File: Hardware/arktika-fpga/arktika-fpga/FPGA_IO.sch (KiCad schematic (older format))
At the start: 12 parts

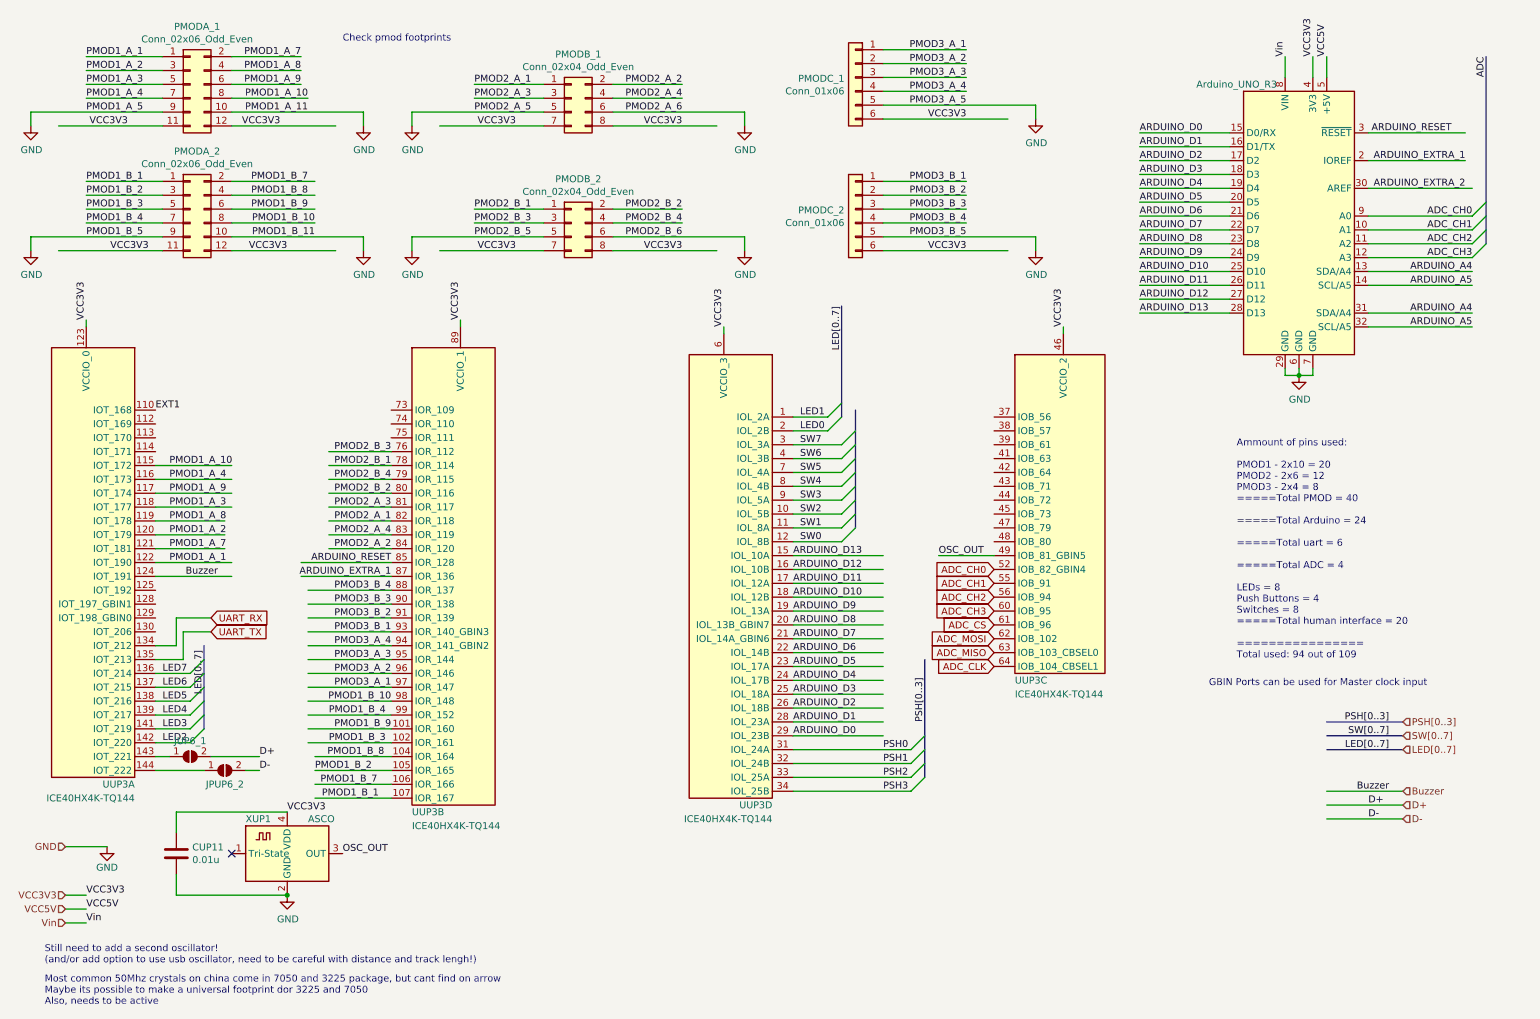
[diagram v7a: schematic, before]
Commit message: Added more IO
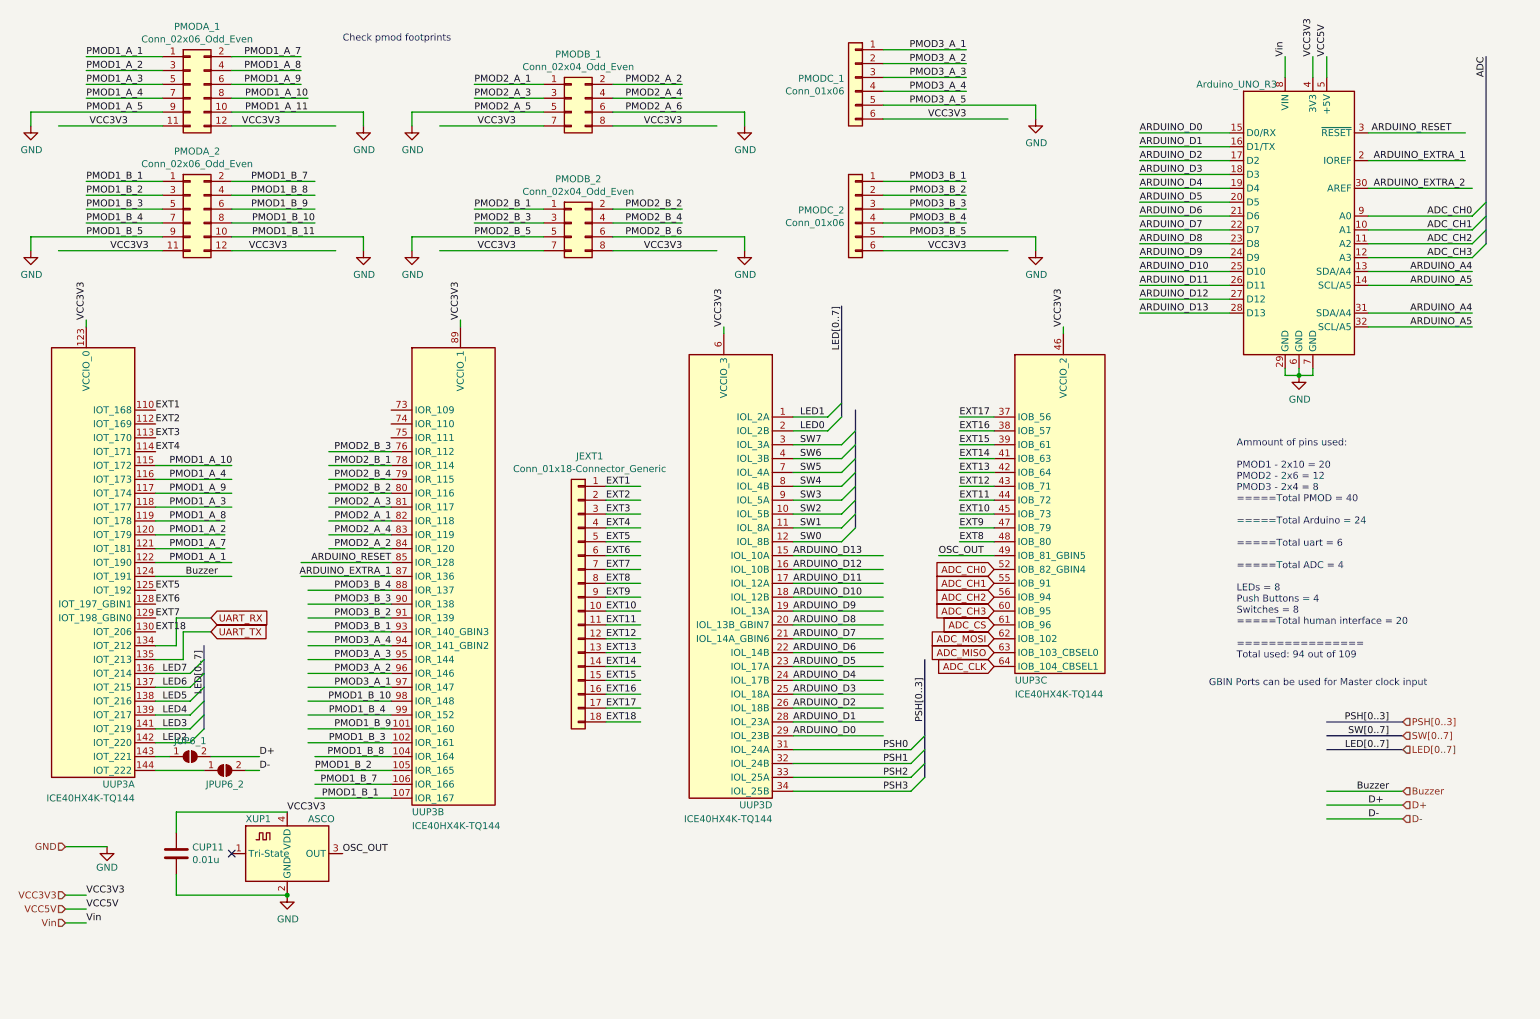
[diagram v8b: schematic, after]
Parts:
- added JEXT1: Conn_01x18-Connector_Generic, Connector_PinHeader_2.54mm:PinHeader_1x18_P2.54mm_Vertical, symbol arktika-fpga-rescue:Conn_01x18-Connector_Generic
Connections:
- net labels added: EXT10, EXT11, EXT12, EXT13, EXT14, EXT15, EXT16, EXT17, EXT18, EXT2, EXT3, EXT4, EXT5, EXT6, EXT7, EXT8, EXT9
- wire segments 190 -> 218
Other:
- note removed: "Most common 50Mhz crystals on china come in 7050 and 3225 package, but cant find on arrow\nMaybe its possible to make a universal footprint dor 3225 and 7050\nAlso, needs to be active"
- note removed: "Still need to add a second oscillator!\n(and/or add option to use usb oscillator, need to be careful with distance and track lengh!)"
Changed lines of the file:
@@
 Wire Wire Line
 	10000 800  10000 950
-Text Notes 750  7350 0    50   ~ 0
-Still need to add a second oscillator!\n(and/or add option to use usb oscillator, need to be careful with distance and track lengh!)
-Text Notes 750  7650 0    50   ~ 0
-Most common 50Mhz crystals on china come in 7050 and 3225 package, but cant find on arrow\nMaybe its possible to make a universal footprint dor 3225 and 7050\nAlso, needs to be active
 $Comp
 L arktika-fpga-rescue:ASCO-Oscillator XUP1
@@
 Text Label 3250 3850 2    50   ~ 0
 PMOD2_B_4
+Text Label 2500 6250 0    50   ~ 0
+VCC3V3
+Text Label 2450 1300 2    50   ~ 0
+VCC3V3
+Text Label 1350 1300 2    50   ~ 0
+VCC3V3
+Text Label 1500 2200 2    50   ~ 0
+VCC3V3
+Text Label 2500 2200 2    50   ~ 0
+VCC3V3
+Text Label 4150 2200 2    50   ~ 0
+VCC3V3
+Text Label 5350 2200 2    50   ~ 0
+VCC3V3
+Text Label 5350 1300 2    50   ~ 0
+VCC3V3
+Text Label 4150 1300 2    50   ~ 0
+VCC3V3
+Text Label 7400 1250 2    50   ~ 0
+VCC3V3
+Text Label 7400 2200 2    50   ~ 0
+VCC3V3
+Text Label 1550 3450 0    50   ~ 0
+EXT2
+Text Label 1550 3550 0    50   ~ 0
+EXT3
+Text Label 1550 3650 0    50   ~ 0
+EXT4
+Text Label 1550 4650 0    50   ~ 0
+EXT5
+Text Label 1550 4750 0    50   ~ 0
+EXT6
+Text Label 1550 4850 0    50   ~ 0
+EXT7
+Text Label 7350 4300 0    50   ~ 0
+EXT8
+Text Label 7350 4200 0    50   ~ 0
+EXT9
+Text Label 7350 4100 0    50   ~ 0
+EXT10
+Text Label 7350 4000 0    50   ~ 0
+EXT11
+Wire Wire Line
+	7350 3400 7600 3400
+Wire Wire Line
+	7350 3500 7600 3500
+Wire Wire Line
+	7600 3600 7350 3600
+Wire Wire Line
+	7350 3700 7600 3700
+Wire Wire Line
+	7350 3800 7600 3800
+Wire Wire Line
+	7350 3900 7600 3900
+Wire Wire Line
+	7600 4000 7350 4000
+Wire Wire Line
+	7350 4100 7600 4100
+Wire Wire Line
+	7600 4200 7350 4200
+Text Label 7350 3900 0    50   ~ 0
+EXT12
+Text Label 7350 3800 0    50   ~ 0
+EXT13
+Text Label 7350 3700 0    50   ~ 0
+EXT14
+Text Label 7350 3600 0    50   ~ 0
+EXT15
+Text Label 7350 3500 0    50   ~ 0
+EXT16
+Text Label 7350 3400 0    50   ~ 0
+EXT17
+Text Label 4800 3900 0    50   ~ 0
+EXT1
+Text Label 4800 4000 0    50   ~ 0
+EXT2
+Text Label 4800 4100 0    50   ~ 0
+EXT3
+Text Label 4800 4200 0    50   ~ 0
+EXT4
+Text Label 4800 4300 0    50   ~ 0
+EXT5
+Text Label 4800 4400 0    50   ~ 0
+EXT6
+Text Label 4800 4500 0    50   ~ 0
+EXT7
+Text Label 4800 4600 0    50   ~ 0
+EXT8
+Text Label 4800 4700 0    50   ~ 0
+EXT9
+Wire Wire Line
+	4800 4700 5050 4700
+Text Label 4800 5500 0    50   ~ 0
+EXT17
+Text Label 4800 5400 0    50   ~ 0
+EXT16
+Text Label 4800 5300 0    50   ~ 0
+EXT15
+Text Label 4800 5200 0    50   ~ 0
+EXT14
+Text Label 4800 5100 0    50   ~ 0
+EXT13
+Text Label 4800 5000 0    50   ~ 0
+EXT12
+Wire Wire Line
+	5050 5500 4800 5500
+Wire Wire Line
+	4800 5400 5050 5400
+Wire Wire Line
+	5050 5300 4800 5300
+Wire Wire Line
+	4800 5200 5050 5200
+Wire Wire Line
+	4800 5100 5050 5100
+Wire Wire Line
+	4800 5000 5050 5000
+Wire Wire Line
+	5050 4900 4800 4900
+Wire Wire Line
+	4800 4800 5050 4800
+Text Label 4800 4900 0    50   ~ 0
+EXT11
+Text Label 4800 4800 0    50   ~ 0
+EXT10
+Wire Wire Line
+	5050 4600 4800 4600
+Wire Wire Line
+	5050 4500 4800 4500
+Wire Wire Line
+	5050 4400 4800 4400
+Wire Wire Line
+	5050 4300 4800 4300
+Wire Wire Line
+	5050 4200 4800 4200
+Wire Wire Line
+	5050 4100 4800 4100
+Wire Wire Line
+	5050 4000 4800 4000
+Wire Wire Line
+	5050 3900 4800 3900
+Wire Wire Line
+	7600 4300 7350 4300
+Text Label 1550 4950 0    50   ~ 0
+EXT18
+$Comp
+L arktika-fpga-rescue:Conn_01x18-Connector_Generic JEXT1
+U 1 1 5F93B780
+P 4600 4700
+F 0 "JEXT1" H 4518 5717 50  0000 C CNN
+F 1 "Conn_01x18-Connector_Generic" H 4518 5626 50  0000 C CNN
+F 2 "Connector_PinHeader_2.54mm:PinHeader_1x18_P2.54mm_Vertical" H 4600 4700 50  0001 C CNN
+F 3 "" H 4600 4700 50  0001 C CNN
+	1    4600 4700
+	-1   0    0    -1
+$EndComp
+Text Label 4800 5600 0    50   ~ 0
+EXT18
+Wire Wire Line
+	5050 5600 4800 5600
 Wire Bus Line
 	6500 2600 6500 3400
@@
 Wire Bus Line
 	6600 3350 6600 4200
-Text Label 2500 6250 0    50   ~ 0
-VCC3V3
-Text Label 2450 1300 2    50   ~ 0
-VCC3V3
-Text Label 1350 1300 2    50   ~ 0
-VCC3V3
-Text Label 1500 2200 2    50   ~ 0
-VCC3V3
-Text Label 2500 2200 2    50   ~ 0
-VCC3V3
-Text Label 4150 2200 2    50   ~ 0
-VCC3V3
-Text Label 5350 2200 2    50   ~ 0
-VCC3V3
-Text Label 5350 1300 2    50   ~ 0
-VCC3V3
-Text Label 4150 1300 2    50   ~ 0
-VCC3V3
-Text Label 7400 1250 2    50   ~ 0
-VCC3V3
-Text Label 7400 2200 2    50   ~ 0
-VCC3V3
 $EndSCHEMATC
